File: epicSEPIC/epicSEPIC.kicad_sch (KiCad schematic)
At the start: 7 parts, among them J1 Entrada 24V, J2 USB Tipo B, J3 Salida 12-48V

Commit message: Actualizar BOM
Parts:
- J1, J3: Dist (none) -> Mouser; DistPN (none) -> 651-1823638; Mfg (none) -> Phoenix Contact; MfgPN (none) -> 1823638; Part Number 1822752 -> (none)
- J2: Dist (none) -> Mouser; DistPN (none) -> 649-61729-0010RLF; Mfg (none) -> Amphenol FCI; MfgPN (none) -> 61729-0010RLF; Part Number 61729-0010RLF -> (none)
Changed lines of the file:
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@@
 			)
 		)
-		(property "Part Number" "61729-0010RLF"
+		(property "Dist" "Mouser"
+			(at 116.84 78.74 0)
+			(effects
+				(font
+					(size 1.27 1.27)
+				)
+				(hide yes)
+			)
+		)
+		(property "DistPN" "649-61729-0010RLF"
+			(at 116.84 78.74 0)
+			(effects
+				(font
+					(size 1.27 1.27)
+				)
+				(hide yes)
+			)
+		)
+		(property "Mfg" "Amphenol FCI"
+			(at 116.84 78.74 0)
+			(effects
+				(font
+					(size 1.27 1.27)
+				)
+				(hide yes)
+			)
+		)
+		(property "MfgPN" "61729-0010RLF"
 			(at 116.84 78.74 0)
 			(effects
@@
 			)
 		)
-		(property "Part Number" "1822752"
+		(property "Dist" "Mouser"
+			(at 204.47 114.3 0)
+			(effects
+				(font
+					(size 1.27 1.27)
+				)
+				(hide yes)
+			)
+		)
+		(property "DistPN" " 651-1823638 "
+			(at 204.47 114.3 0)
+			(effects
+				(font
+					(size 1.27 1.27)
+				)
+				(hide yes)
+			)
+		)
+		(property "Mfg" "Phoenix Contact"
+			(at 204.47 114.3 0)
+			(effects
+				(font
+					(size 1.27 1.27)
+				)
+				(hide yes)
+			)
+		)
+		(property "MfgPN" "1823638"
 			(at 204.47 114.3 0)
 			(effects
@@
 			)
 		)
+		(property "Dist" ""
+			(at 290.83 421.64 0)
+			(effects
+				(font
+					(size 1.27 1.27)
+				)
+				(hide yes)
+			)
+		)
+		(property "DistPN" ""
+			(at 290.83 421.64 0)
+			(effects
+				(font
+					(size 1.27 1.27)
+				)
+				(hide yes)
+			)
+		)
+		(property "Mfg" ""
+			(at 290.83 421.64 0)
+			(effects
+				(font
+					(size 1.27 1.27)
+				)
+				(hide yes)
+			)
+		)
 		(instances
 			(project "epicSEPIC"
@@
 			)
 		)
-		(property "Part Number" "1822752"
+		(property "Dist" "Mouser"
+			(at 102.87 116.84 0)
+			(effects
+				(font
+					(size 1.27 1.27)
+				)
+				(hide yes)
+			)
+		)
+		(property "DistPN" " 651-1823638 "
+			(at 102.87 116.84 0)
+			(effects
+				(font
+					(size 1.27 1.27)
+				)
+				(hide yes)
+			)
+		)
+		(property "Mfg" "Phoenix Contact"
+			(at 102.87 116.84 0)
+			(effects
+				(font
+					(size 1.27 1.27)
+				)
+				(hide yes)
+			)
+		)
+		(property "MfgPN" "1823638"
 			(at 102.87 116.84 0)
 			(effects
@@
 			)
 		)
+		(property "Dist" ""
+			(at 290.83 416.56 0)
+			(effects
+				(font
+					(size 1.27 1.27)
+				)
+				(hide yes)
+			)
+		)
+		(property "DistPN" ""
+			(at 290.83 416.56 0)
+			(effects
+				(font
+					(size 1.27 1.27)
+				)
+				(hide yes)
+			)
+		)
+		(property "Mfg" ""
+			(at 290.83 416.56 0)
+			(effects
+				(font
+					(size 1.27 1.27)
+				)
+				(hide yes)
+			)
+		)
 		(instances
 			(project ""
@@
 			)
 		)
+		(property "Dist" ""
+			(at 290.83 426.72 0)
+			(effects
+				(font
+					(size 1.27 1.27)
+				)
+				(hide yes)
+			)
+		)
+		(property "DistPN" ""
+			(at 290.83 426.72 0)
+			(effects
+				(font
+					(size 1.27 1.27)
+				)
+				(hide yes)
+			)
+		)
+		(property "Mfg" ""
+			(at 290.83 426.72 0)
+			(effects
+				(font
+					(size 1.27 1.27)
+				)
+				(hide yes)
+			)
+		)
 		(instances
 			(project "epicSEPIC"
@@
 			(at 290.83 431.8 0)
 			(effects
+				(font
+					(size 1.27 1.27)
+				)
+				(hide yes)
+			)
+		)
+		(property "Dist" ""
+			(at 290.83 431.8 0)
+			(effects
+				(font
+					(size 1.27 1.27)
+				)
+				(hide yes)
+			)
+		)
+		(property "DistPN" ""
+			(at 290.83 431.8 0)
+			(effects
+				(font
+					(size 1.27 1.27)
+				)
+				(hide yes)
+			)
+		)
+		(property "Mfg" ""
+			(at 290.83 431.8 0)
+			(effects

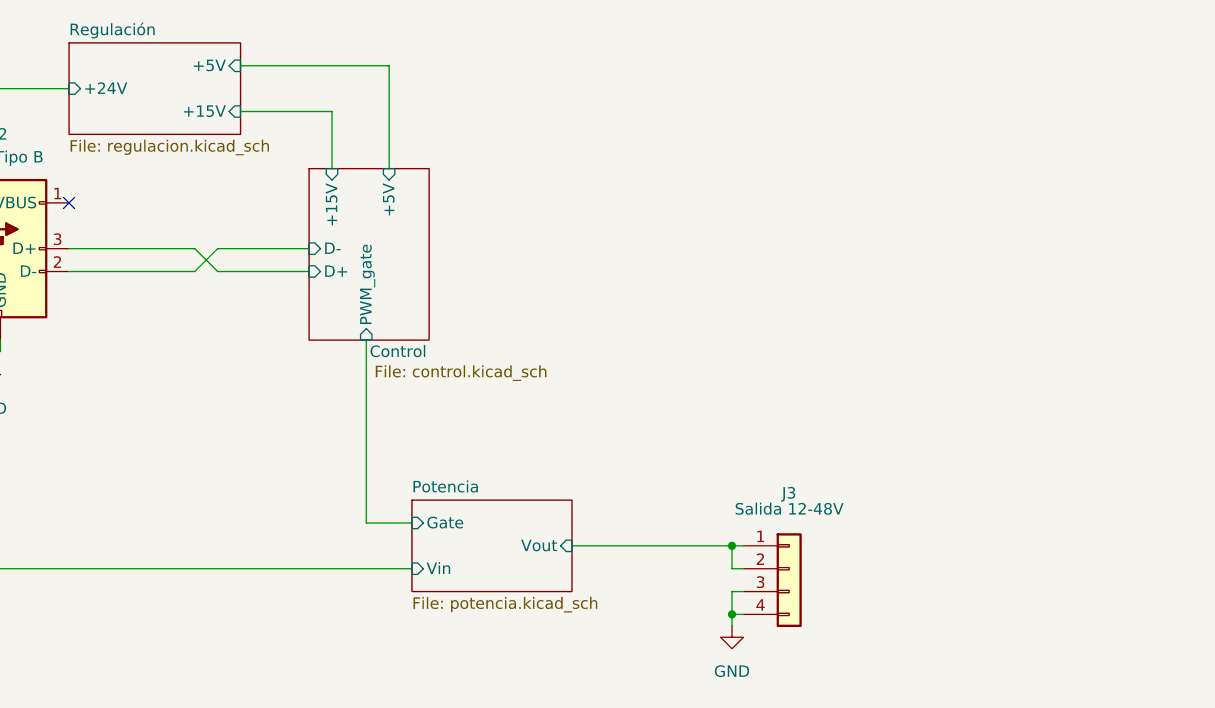
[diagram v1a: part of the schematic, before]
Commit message: Agregar ESP32 a pcb
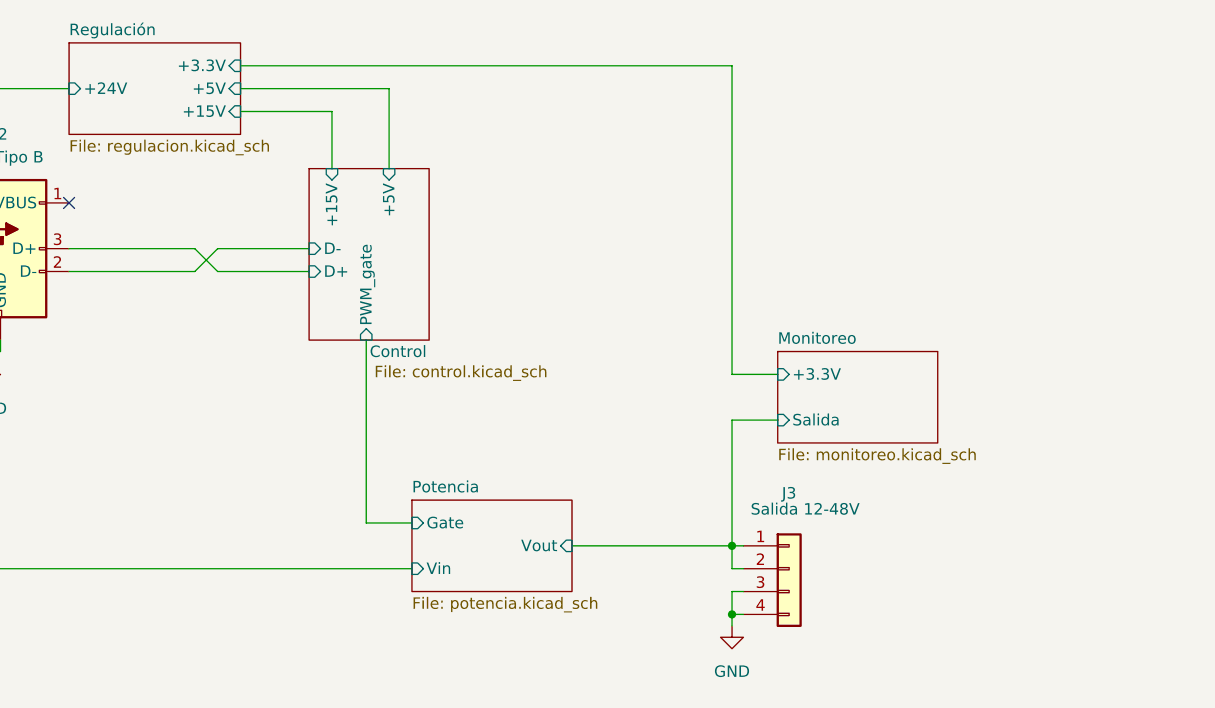
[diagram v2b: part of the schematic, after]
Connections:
- net Potencia/Vout renamed Monitoreo/Salida
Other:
- added sheet Monitoreo (monitoreo.kicad_sch)
- sheet Regulación ports: added +3.3V; removed none
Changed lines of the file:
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@@
+	(wire
+		(pts
+			(xy 203.2 97.79) (xy 198.12 97.79)
+		)
+		(stroke
+			(width 0)
+			(type default)
+		)
+	)
+	(wire
+		(pts
+			(xy 198.12 92.71) (xy 203.2 92.71)
+		)
+		(stroke
+			(width 0)
+			(type default)
+		)
+	)
 	(wire
 		(pts
@@
 	(wire
 		(pts
+			(xy 143.51 58.42) (xy 198.12 58.42)
+		)
+		(stroke
+			(width 0)
+			(type default)
+		)
+	)
+	(wire
+		(pts
 			(xy 180.34 111.76) (xy 198.12 111.76)
 		)
@@
 	(wire
 		(pts
+			(xy 198.12 58.42) (xy 198.12 92.71)
+		)
+		(stroke
+			(width 0)
+			(type default)
+		)
+	)
+	(wire
+		(pts
 			(xy 115.57 90.17) (xy 115.57 91.44)
 		)
@@
 	(wire
 		(pts
+			(xy 160.02 60.96) (xy 160.02 69.85)
+		)
+		(stroke
+			(width 0)
+			(type default)
+		)
+	)
+	(wire
+		(pts
 			(xy 143.51 63.5) (xy 153.67 63.5)
 		)
@@
 	(wire
 		(pts
-			(xy 143.51 58.42) (xy 160.02 58.42)
+			(xy 143.51 60.96) (xy 160.02 60.96)
 		)
 		(stroke
@@
 	(wire
 		(pts
-			(xy 160.02 58.42) (xy 160.02 69.85)
-		)
-		(stroke
-			(width 0)
-			(type default)
-		)
-	)
-	(wire
-		(pts
 			(xy 116.84 90.17) (xy 116.84 88.9)
+		)
+		(stroke
+			(width 0)
+			(type default)
+		)
+	)
+	(wire
+		(pts
+			(xy 198.12 97.79) (xy 198.12 111.76)
 		)
 		(stroke
@@
 			)
 		)
-		(property "Description" "USB Type B connector"
+		(property "Description" "Conector USB Tipo B"
 			(at 116.84 78.74 0)
 			(effects
@@
 		)
 		(property "Value" "Salida 12-48V"
-			(at 204.47 107.696 0)
+			(at 206.248 107.696 0)
 			(effects
 				(font
@@
 			)
 		)
-		(property "Description" "Generic connector, single row, 01x04, script generated (kicad-library-utils/schlib/autogen/connector/)"
+		(property "Description" "Bloque de terminales, 2 polos, con resorte"
 			(at 204.47 114.3 0)
 			(effects
@@
 			)
 		)
-		(property "Description" "Generic connector, single row, 01x04, script generated (kicad-library-utils/schlib/autogen/connector/)"
+		(property "Description" "Bloque de terminales, 2 polos, con resorte"
 			(at 102.87 116.84 0)
 			(effects
@@
 		)
 		(pin "+5V" input
-			(at 143.51 58.42 0)
+			(at 143.51 60.96 0)
 			(effects
 				(font
@@
 				)
 				(justify left)
+			)
+		)
+		(pin "+3.3V" input
+			(at 143.51 58.42 0)
+			(effects
+				(font
+					(size 1.27 1.27)
+				)
+				(justify right)
 			)
 		)
@@
 				)
 			)
+		)
+	)
+	(sheet
+		(at 203.2 90.17)
+		(size 17.78 10.16)
+		(exclude_from_sim no)
+		(in_bom yes)
+		(on_board yes)
+		(dnp no)
+		(fields_autoplaced yes)
+		(stroke
+			(width 0.1524)
+			(type solid)
+		)
+		(fill
+			(color 0 0 0 0.0000)
+		)
+		(property "Sheetname" "Monitoreo"
+			(at 203.2 89.4584 0)
+			(effects
+				(font
+					(size 1.27 1.27)
+				)
+				(justify left bottom)
+			)
+		)
+		(property "Sheetfile" "monitoreo.kicad_sch"
+			(at 203.2 100.9146 0)
+			(effects
+				(font
+					(size 1.27 1.27)
+				)
+				(justify left top)
+			)
+		)
+		(pin "+3.3V" input
+			(at 203.2 92.71 180)
+			(effects
+				(font
+					(size 1.27 1.27)
+				)
+				(justify left)
+			)
+		)
+		(pin "Salida" input
+			(at 203.2 97.79 180)
+			(effects
+				(font
+					(size 1.27 1.27)
+				)
+				(justify left)
+			)
+		)
+		(instances
+			(project "epicSEPIC"
+				(path "/4aad8e32-74ba-4d05-8827-a4f531fce32b"
+					(page "5")
+				)
+			)
